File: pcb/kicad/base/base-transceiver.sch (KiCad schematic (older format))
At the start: 4 parts, among them U2 XBee-PRO_900HP

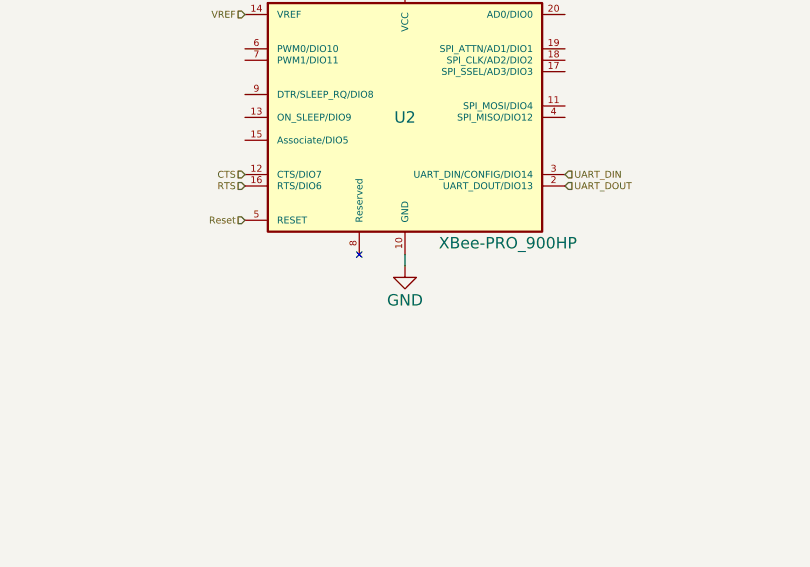
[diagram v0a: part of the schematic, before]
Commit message: Update display and XBee position once more
GPIO pins were rearranged to achieve a tighter fit on the available
components. Patch antenna is now replaced with SMA connector for first
prototype. Buttons will be simulated with a pin header short. Audio
speaker is planned to go below the display, perhpas on the side of the
housing.
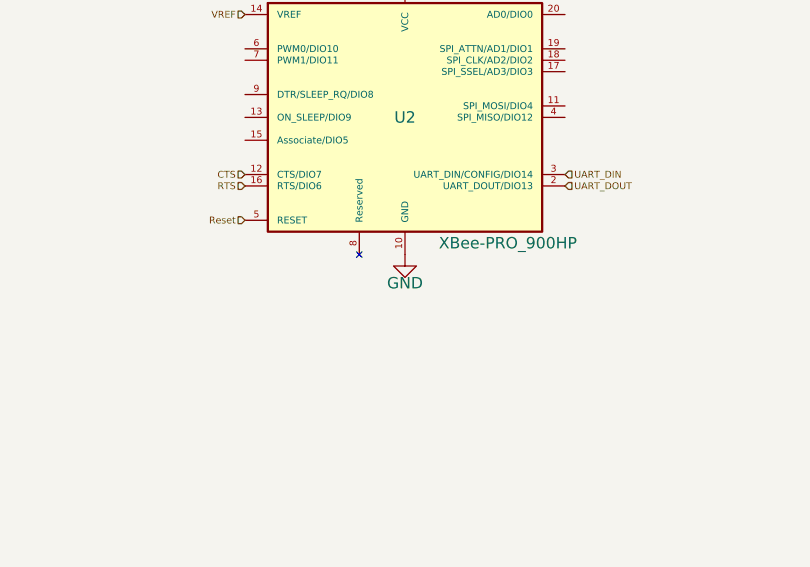
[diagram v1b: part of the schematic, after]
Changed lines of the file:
@@
 L GND #PWR025
 U 1 1 58C1BBBE
-P 5850 4150
-F 0 "#PWR025" H 5850 3900 50  0001 C CNN
-F 1 "GND" H 5850 4000 50  0000 C CNN
-F 2 "" H 5850 4150 50  0000 C CNN
-F 3 "" H 5850 4150 50  0000 C CNN
-	1    5850 4150
+P 5850 4100
+F 0 "#PWR025" H 5850 3850 50  0001 C CNN
+F 1 "GND" H 5850 3975 50  0000 C CNN
+F 2 "" H 5850 4100 50  0000 C CNN
+F 3 "" H 5850 4100 50  0000 C CNN
+	1    5850 4100
 	1    0    0    -1
 $EndComp
-Wire Wire Line
-	5850 4100 5850 4150
 $Comp
 L C_Small C20
